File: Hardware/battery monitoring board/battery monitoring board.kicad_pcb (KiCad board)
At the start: 4 copper layers, 142 x 53.3 mm, 71 parts, among them J1 Conn_01x02, J10 9V Conn_01x02, J2 Conn_01x02, J3 S5B-XH-A, J4 Conn_01x02, J5 Conn_01x02, J6 Conn_01x02, J7 Conn_01x02, J8 Conn_01x02, J9 S5B-XH-A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

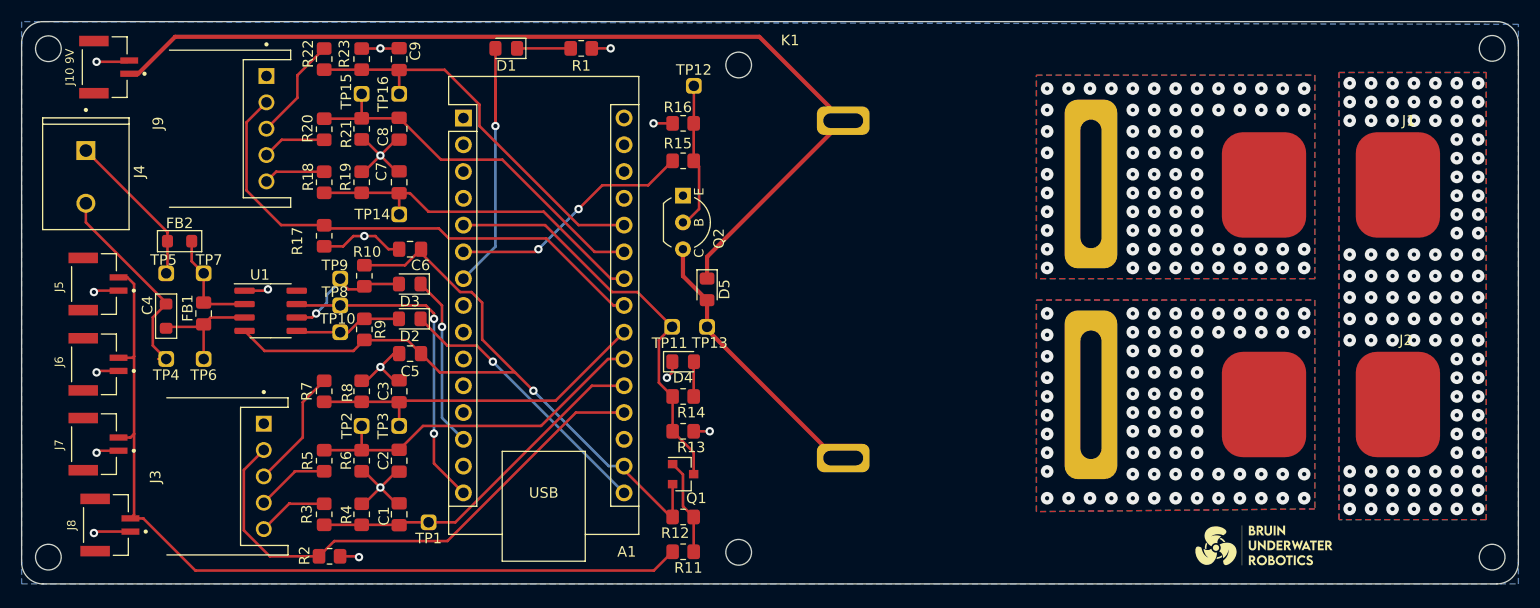
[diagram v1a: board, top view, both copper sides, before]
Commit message: Update battery monitoring board.kicad_pcb
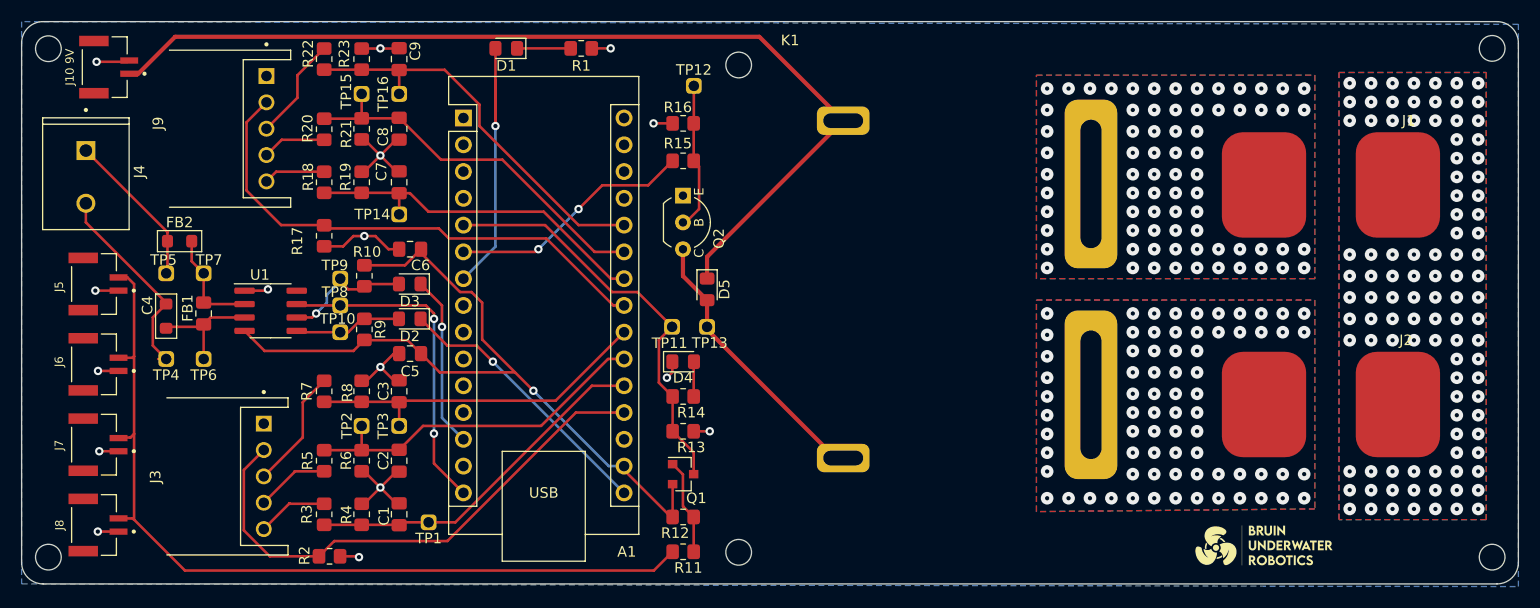
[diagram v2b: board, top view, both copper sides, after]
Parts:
- moved J8 1.13 mm to (88.4, 68.1)
- moved J7 0.05 mm to (88.4, 60.5)
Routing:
- net GND: track 62.6 -> 60.0 mm
- net /leak sensor/PROBE: track 81.5 -> 82.9 mm
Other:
- copper layers 4 -> 2
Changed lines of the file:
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@@
   (layers
     (0 "F.Cu" signal)
-    (1 "In1.Cu" signal)
-    (2 "In2.Cu" signal)
     (31 "B.Cu" signal)
     (32 "B.Adhes" user "B.Adhesive")
@@
       (layer "F.Mask" (type "Top Solder Mask") (thickness 0.01))
       (layer "F.Cu" (type "copper") (thickness 0.035))
-      (layer "dielectric 1" (type "prepreg") (thickness 0.1) (material "FR4") (epsilon_r 4.5) (loss_tangent 0.02))
-      (layer "In1.Cu" (type "copper") (thickness 0.035))
-      (layer "dielectric 2" (type "core") (thickness 1.24) (material "FR4") (epsilon_r 4.5) (loss_tangent 0.02))
-      (layer "In2.Cu" (type "copper") (thickness 0.035))
-      (layer "dielectric 3" (type "prepreg") (thickness 0.1) (material "FR4") (epsilon_r 4.5) (loss_tangent 0.02))
+      (layer "dielectric 1" (type "core") (thickness 1.51) (material "FR4") (epsilon_r 4.5) (loss_tangent 0.02))
       (layer "B.Cu" (type "copper") (thickness 0.035))
       (layer "B.Mask" (type "Bottom Solder Mask") (thickness 0.01))
@@
     (property "ki_keywords" "L ferrite bead inductor filter")
     (attr smd)
-    (fp_text reference "FB2" (at 0 -1.7) (layer "F.SilkS")
+    (fp_text reference "FB2" (at 0 -1.778) (layer "F.SilkS")
         (effects (font (size 1 1) (thickness 0.15)))
     )
@@
   )
   (footprint "Library:JST_BM02B-GHS-TBT_LF__SN_" (layer "F.Cu")
-    (at 89.5235 68.072 -90)
+    (at 88.392 68.072 -90)
     (property "Sheetfile" "leak sensor.kicad_sch")
     (property "Sheetname" "leak sensor")
@@
   )
   (footprint "Library:JST_BM02B-GHS-TBT_LF__SN_" (layer "F.Cu")
-    (at 88.392 60.400603 -90)
+    (at 88.392 60.452 -90)
     (property "Sheetfile" "leak sensor.kicad_sch")
     (property "Sheetname" "leak sensor")
@@
   (segment (start 118.3635 51.816) (end 117.856 51.816) (width 0.25) (layer "F.Cu") (net 4))
   (segment (start 118.364 66.0185) (end 118.0885 66.0185) (width 0.25) (layer "F.Cu") (net 4))
-  (segment (start 89.799 53.457) (end 89.662 53.594) (width 0.25) (layer "F.Cu") (net 4))
-  (segment (start 91.742 61.025603) (end 89.850397 61.025603) (width 0.25) (layer "F.Cu") (net 4))
   (segment (start 136.636 22.86) (end 138.43 22.86) (width 0.25) (layer "F.Cu") (net 4))
   (segment (start 89.662 24.13) (end 92.641 24.13) (width 0.25) (layer "F.Cu") (net 4))
+  (segment (start 89.916 60.96) (end 89.916 61.077) (width 0.25) (layer "F.Cu") (net 4))
   (segment (start 113.046 41.64) (end 111.252 41.64) (width 0.25) (layer "F.Cu") (net 4))
   (segment (start 116.0995 40.6615) (end 117.348 41.91) (width 0.25) (layer "F.Cu") (net 4))
   (segment (start 116.586 22.86) (end 116.602 22.876) (width 0.25) (layer "F.Cu") (net 4))
-  (segment (start 93.3815 68.697) (end 89.545 68.697) (width 0.25) (layer "F.Cu") (net 4))
+  (segment (start 89.545 45.837) (end 91.742 45.837) (width 0.25) (layer "F.Cu") (net 4))
   (segment (start 114.0245 40.6615) (end 113.046 41.64) (width 0.25) (layer "F.Cu") (net 4))
   (segment (start 114.47583 71.04183) (end 114.554 71.12) (width 0.25) (layer "F.Cu") (net 4))
@@
   (segment (start 118.0885 63.0135) (end 116.586 64.516) (width 0.25) (layer "F.Cu") (net 4))
   (segment (start 103.697 45.847) (end 105.791 45.847) (width 0.25) (layer "F.Cu") (net 4))
-  (segment (start 89.545 45.837) (end 89.408 45.974) (width 0.25) (layer "F.Cu") (net 4))
   (segment (start 115.046 34.56) (end 116.586 33.02) (width 0.25) (layer "F.Cu") (net 4))
   (segment (start 114.808 22.876) (end 116.57 22.876) (width 0.25) (layer "F.Cu") (net 4))
   (segment (start 115.046 66.056) (end 116.586 64.516) (width 0.25) (layer "F.Cu") (net 4))
-  (segment (start 89.850397 61.025603) (end 89.662 61.214) (width 0.25) (layer "F.Cu") (net 4))
   (segment (start 118.364 54.3505) (end 117.8505 54.3505) (width 0.25) (layer "F.Cu") (net 4))
   (segment (start 114.808 31.496) (end 115.062 31.496) (width 0.25) (layer "F.Cu") (net 4))
-  (segment (start 89.545 68.697) (end 89.408 68.834) (width 0.25) (layer "F.Cu") (net 4))
   (segment (start 117.856 51.816) (end 116.586 53.086) (width 0.25) (layer "F.Cu") (net 4))
   (segment (start 115.062 40.6615) (end 116.0995 40.6615) (width 0.25) (layer "F.Cu") (net 4))
+  (segment (start 91.742 61.077) (end 89.916 61.077) (width 0.25) (layer "F.Cu") (net 4))
+  (segment (start 89.779 68.697) (end 91.742 68.697) (width 0.25) (layer "F.Cu") (net 4))
   (segment (start 116.602 22.876) (end 118.3265 22.876) (width 0.25) (layer "F.Cu") (net 4))
   (segment (start 146.304 59.182) (end 147.828 59.182) (width 0.25) (layer "F.Cu") (net 4))
@@
   (segment (start 118.364 63.0135) (end 118.0885 63.0135) (width 0.25) (layer "F.Cu") (net 4))
   (segment (start 118.0885 34.5225) (end 116.586 33.02) (width 0.25) (layer "F.Cu") (net 4))
-  (segment (start 91.742 45.837) (end 89.545 45.837) (width 0.25) (layer "F.Cu") (net 4))
-  (segment (start 91.742 53.457) (end 89.799 53.457) (width 0.25) (layer "F.Cu") (net 4))
+  (segment (start 89.799 53.457) (end 91.742 53.457) (width 0.25) (layer "F.Cu") (net 4))
   (segment (start 118.3265 22.876) (end 118.364 22.8385) (width 0.25) (layer "F.Cu") (net 4))
   (segment (start 114.808 54.388) (end 115.284 54.388) (width 0.25) (layer "F.Cu") (net 4))
@@
   (via (at 220.726 62.992) (size 1.2) (drill 0.4) (layers "F.Cu" "B.Cu") (net 4))
   (via (at 212.598 44.45) (size 1.2) (drill 0.4) (layers "F.Cu" "B.Cu") (net 4))
+  (via (at 89.916 61.077) (size 0.8) (drill 0.4) (layers "F.Cu" "B.Cu") (net 4))
   (via (at 218.694 46.482) (size 1.2) (drill 0.4) (layers "F.Cu" "B.Cu") (net 4))
   (via (at 214.63 48.514) (size 1.2) (drill 0.4) (layers "F.Cu" "B.Cu") (net 4))
@@
   (via (at 220.726 44.45) (size 1.2) (drill 0.4) (layers "F.Cu" "B.Cu") (net 4))
   (via (at 218.694 36.83) (size 1.2) (drill 0.4) (layers "F.Cu" "B.Cu") (net 4))
-  (via (at 89.662 53.594) (size 0.8) (drill 0.4) (layers "F.Cu" "B.Cu") (free) (net 4))
+  (via (at 89.799 53.457) (size 0.8) (drill 0.4) (layers "F.Cu" "B.Cu") (free) (net 4))
   (via (at 220.726 36.83) (size 1.2) (drill 0.4) (layers "F.Cu" "B.Cu") (net 4))
   (via (at 208.534 42.418) (size 1.2) (drill 0.4) (layers "F.Cu" "B.Cu") (net 4))
@@
   (via (at 210.566 50.546) (size 1.2) (drill 0.4) (layers "F.Cu" "B.Cu") (net 4))
   (via (at 208.534 29.718) (size 1.2) (drill 0.4) (layers "F.Cu" "B.Cu") (net 4))
-  (via (at 89.662 61.214) (size 0.8) (drill 0.4) (layers "F.Cu" "B.Cu") (free) (net 4))
   (via (at 116.586 53.086) (size 0.8) (drill 0.4) (layers "F.Cu" "B.Cu") (free) (net 4))
   (via (at 216.662 44.45) (size 1.2) (drill 0.4) (layers "F.Cu" "B.Cu") (net 4))
@@
   (via (at 210.566 29.718) (size 1.2) (drill 0.4) (layers "F.Cu" "B.Cu") (net 4))
   (via (at 89.662 24.13) (size 0.8) (drill 0.4) (layers "F.Cu" "B.Cu") (free) (net 4))
-  (via (at 89.408 45.974) (size 0.8) (drill 0.4) (layers "F.Cu" "B.Cu") (free) (net 4))
+  (via (at 89.545 45.837) (size 0.8) (drill 0.4) (layers "F.Cu" "B.Cu") (free) (net 4))
   (via (at 210.566 44.45) (size 1.2) (drill 0.4) (layers "F.Cu" "B.Cu") (net 4))
-  (via (at 89.408 68.834) (size 0.8) (drill 0.4) (layers "F.Cu" "B.Cu") (free) (net 4))
+  (via (at 89.779 68.697) (size 0.8) (drill 0.4) (layers "F.Cu" "B.Cu") (free) (net 4))
   (via (at 208.534 44.45) (size 1.2) (drill 0.4) (layers "F.Cu" "B.Cu") (net 4))
   (via (at 214.63 44.45) (size 1.2) (drill 0.4) (layers "F.Cu" "B.Cu") (net 4))
@@
   (segment (start 92.593 44.587) (end 91.742 44.587) (width 0.25) (layer "F.Cu") (net 45))
   (segment (start 91.742 59.775603) (end 92.878397 59.775603) (width 0.25) (layer "F.Cu") (net 45))
-  (segment (start 92.8735 67.447) (end 93.218 67.1025) (width 0.25) (layer "F.Cu") (net 45))
-  (segment (start 92.8735 67.447) (end 94.092 67.447) (width 0.25) (layer "F.Cu") (net 45))
+  (segment (start 142.526 72.39) (end 144.304 70.612) (width 0.25) (layer "F.Cu") (net 45))
   (segment (start 93.218 59.436) (end 93.218 52.07) (width 0.25) (layer "F.Cu") (net 45))
   (segment (start 92.878397 59.775603) (end 93.218 59.436) (width 0.25) (layer "F.Cu") (net 45))
   (segment (start 93.218 52.07) (end 93.218 45.212) (width 0.25) (layer "F.Cu") (net 45))
-  (segment (start 144.304 70.612) (end 142.526 72.39) (width 0.25) (layer "F.Cu") (net 45))
-  (segment (start 93.218 67.1025) (end 93.218 59.436) (width 0.25) (layer "F.Cu") (net 45))
-  (segment (start 142.526 72.39) (end 99.035 72.39) (width 0.25) (layer "F.Cu") (net 45))
+  (segment (start 93.218 67.564) (end 93.218 59.436) (width 0.25) (layer "F.Cu") (net 45))
   (segment (start 93.081 52.207) (end 93.218 52.07) (width 0.25) (layer "F.Cu") (net 45))
-  (segment (start 99.035 72.39) (end 94.0945 67.4495) (width 0.25) (layer "F.Cu") (net 45))
   (segment (start 93.218 45.212) (end 92.593 44.587) (width 0.25) (layer "F.Cu") (net 45))
+  (segment (start 98.044 72.39) (end 142.526 72.39) (width 0.25) (layer "F.Cu") (net 45))
   (segment (start 91.742 52.207) (end 93.081 52.207) (width 0.25) (layer "F.Cu") (net 45))
-  (segment (start 94.092 67.447) (end 94.0945 67.4495) (width 0.25) (layer "F.Cu") (net 45))
+  (segment (start 93.101 67.447) (end 98.044 72.39) (width 0.25) (layer "F.Cu") (net 45))
+  (segment (start 91.6035 67.447) (end 93.101 67.447) (width 0.25) (layer "F.Cu") (net 45))
+  (segment (start 93.101 67.447) (end 93.218 67.564) (width 0.25) (layer "F.Cu") (net 45))
   (segment (start 105.776 30.48) (end 108.712 27.544) (width 0.25) (layer "F.Cu") (net 46))
   (segment (start 108.712 27.544) (end 108.712 25.416) (width 0.25) (layer "F.Cu") (net 46))
@@
     (polygon
       (pts
-        (xy 224.536 73.66)
+        (xy 224.536 73.914)
         (xy 224.536 20.574)
         (xy 82.55 20.32)

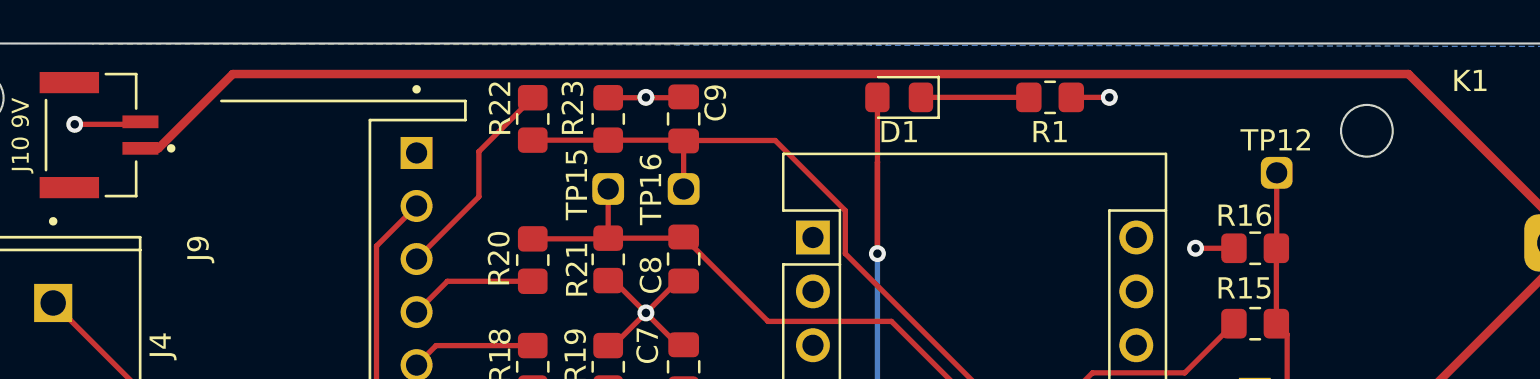
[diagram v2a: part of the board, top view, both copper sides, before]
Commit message: connected Vin to 9V battery
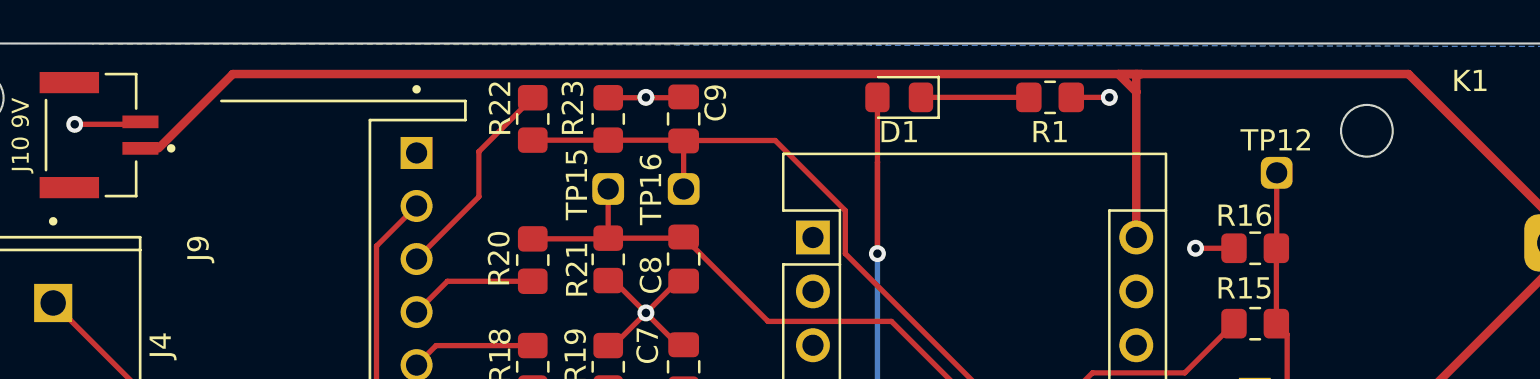
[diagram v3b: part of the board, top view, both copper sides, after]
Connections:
- A1 pad 30: unconnected-(A1-VIN-Pad30) -> Net-(D5-K)
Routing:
- net Net-(D5-K): track 93.2 -> 102.0 mm

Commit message: silkscreen
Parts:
- removed J10 9V: Conn_01x02, Library:JST_BM02B-GHS-TBT_LF__SN_
- added J10: Conn_01x02, Library:JST_BM02B-GHS-TBT_LF__SN_, F.Cu at (89.4, 24.9)
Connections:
- net Net-(D5-K) renamed +9V
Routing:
- net +9V: track 102.0 -> 102.9 mm
- net GND: track 60.0 -> 59.3 mm
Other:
- outline, holes or cut-outs redrawn
- board text added: "9V"
- board text added: "Battery Monitoring Board v1 12/23/2023"
